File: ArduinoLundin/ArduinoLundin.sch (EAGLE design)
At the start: 24 parts, among them Q1 #MHz, U1 ATMEGA168#, U2 ###V

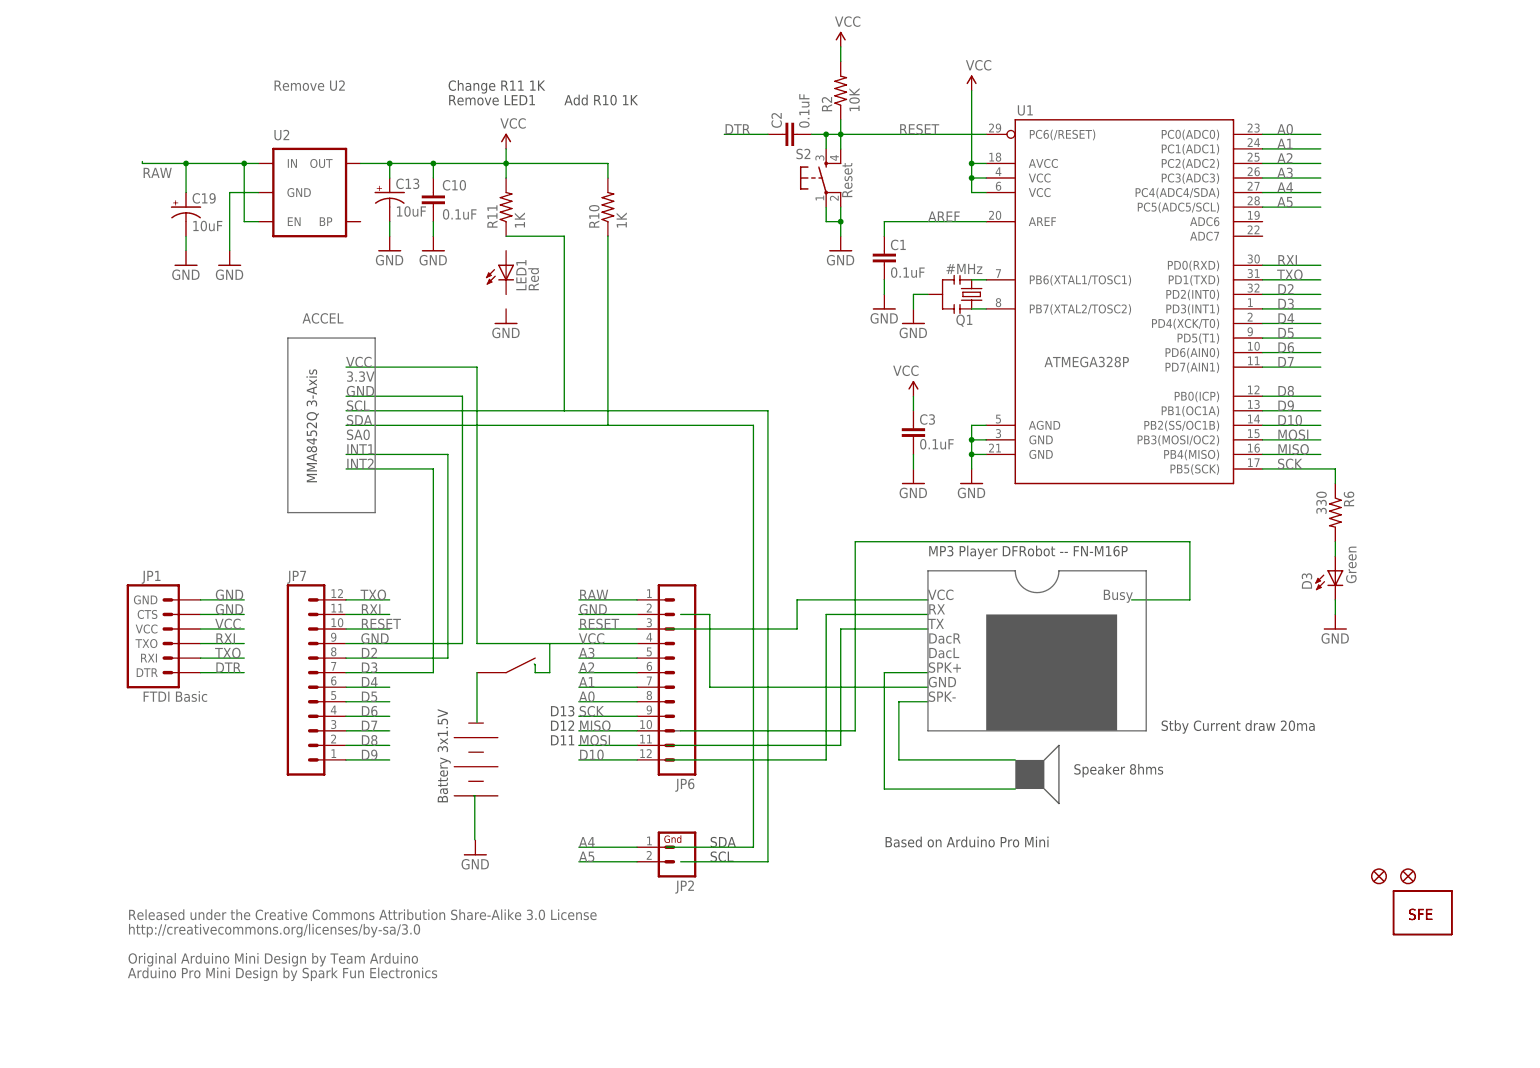
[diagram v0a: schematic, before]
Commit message: added power down option for MP3 and USB connector
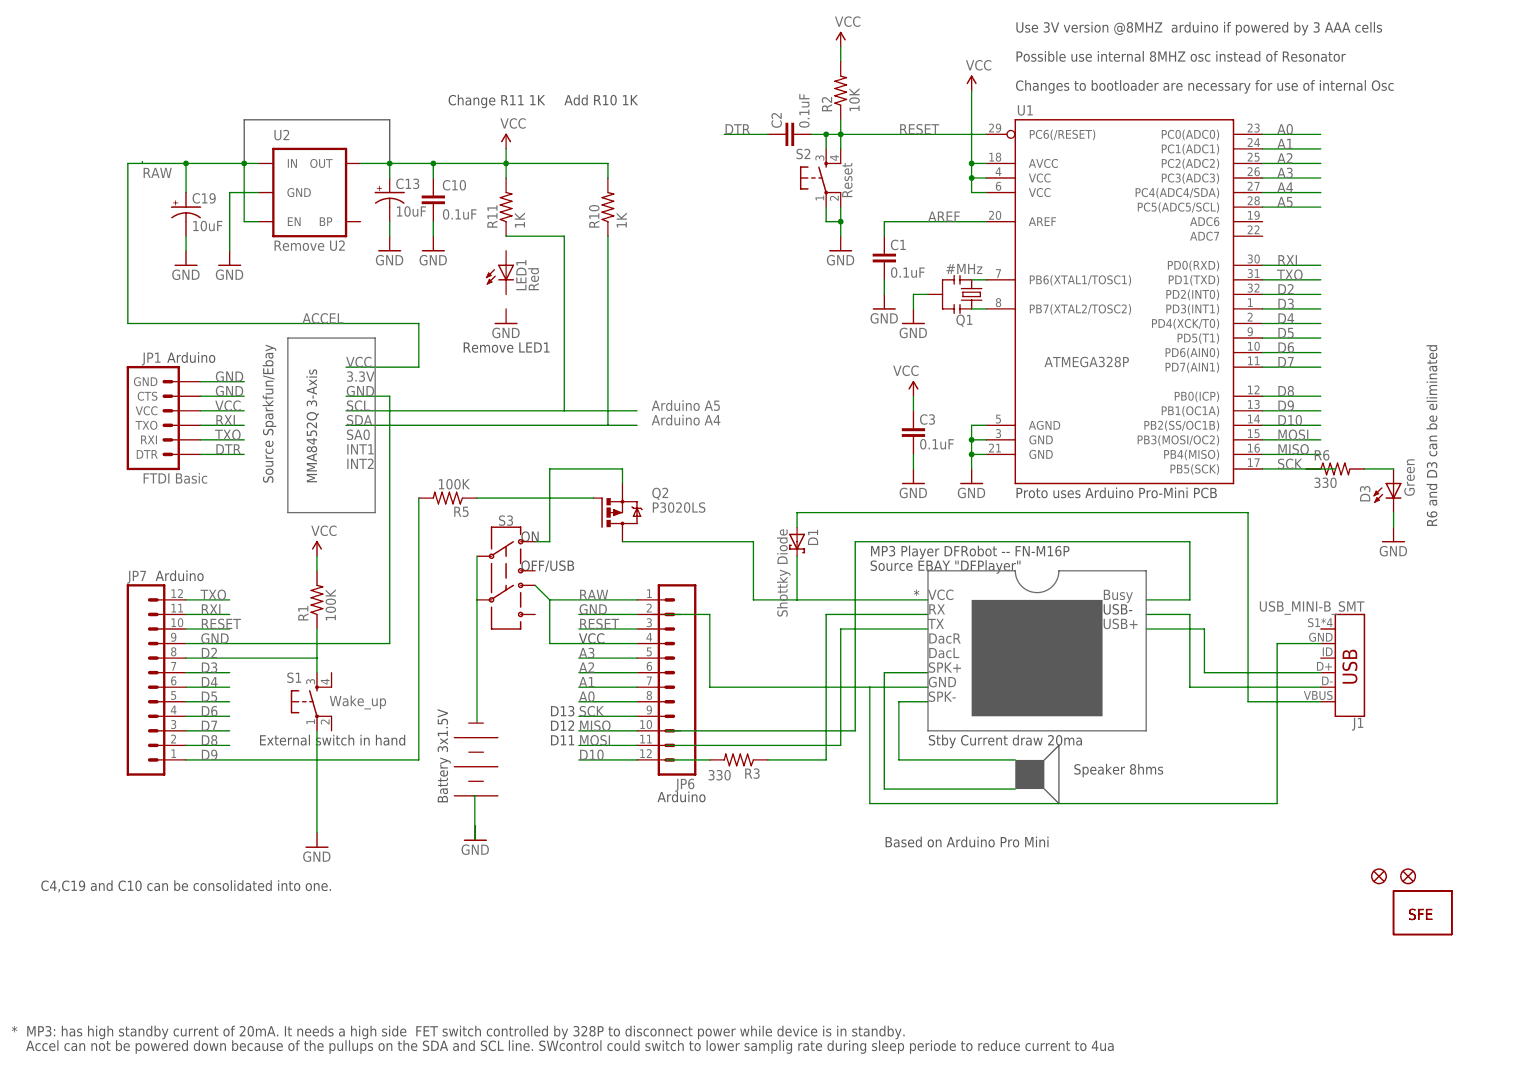
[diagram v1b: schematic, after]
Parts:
- removed JP2: (no value), SparkFun:M02PTH
- added D1: Shottky Diode, diode:BAS40
- added J1: USB_MINI-B_SMT, SparkFun-Connectors:USB_MINI-B_SMT
- added Q2: P3020LS, transistor-power:IRFR5305
- added R1, R5: 100K, SparkFun:RESISTOR0402
- added R3: 330, SparkFun:RESISTOR0402
- added S1: Wake_up, SparkFun:TAC_SWITCHSND
- added S3: (no value), SparkFun-Switches:SWITCH-DPDT-SMD-AYZ0202
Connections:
- new net 3.3V: R1.2
- new net N$11: D1.A, J1.VBUS
- new net N$12: R3.1
- new net N$16: S3.2, S3.5
- new net N$18: J1.D-
- new net N$19: J1.D+
- new net N$22: Q2.S, S3.1
- new net N$3: Q2.G, R5.1
- new net N$5: R3.2
- new net N$9: J1.GND
- net A4: no longer JP2.1
- net A5: no longer JP2.2
- net D2: now also R1.1, S1.3
- net D9: now also R5.2
- net GND: now also S1.1
- net RAW: now also JP6.4, S3.4
- net VCC: now also D1.C, Q2.D; no longer JP6.4
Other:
- note added: "*"
- note added: "Accel can not be powered down because of the pullups on the SDA and SCL line. SWcontrol could switch to lower samplig rate during sleep periode to reduce current to 4ua"
- note added: "Arduino"
- note added: "Arduino A4"
- note added: "Arduino A5"
- note added: "C4,C19 and C10 can be consolidated into one."
- note added: "Changes to bootloader are necessary for use of internal Osc"
- note added: "External switch in hand"
- note added: "MP3: has high standby current of 20mA. It needs a high side FET switch controlled by 328P to disconnect power while device is in standby."
- note added: "OFF/USB"
- note added: "ON"
- note added: "Possible use internal 8MHZ osc instead of Resonator"
- note added: "Proto uses Arduino Pro-Mini PCB"
- note added: "R6 and D3 can be eliminated"
- note added: "Source EBAY "DFPlayer""
- note added: "Source Sparkfun/Ebay"
- note added: "USB+"
- note added: "USB-"
- note added: "Use 3V version @8MHZ arduino if powered by 3 AAA cells"
- note removed: "Arduino Pro Mini Design by Spark Fun Electronics"
- note removed: "Original Arduino Mini Design by Team Arduino"
- note removed: "Released under the Creative Commons Attribution Share-Alike 3.0 License"
- note removed: "http://creativecommons.org/licenses/by-sa/3.0"
- moved on the sheet: D3, JP1, JP7, R6

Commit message: hopefully last changes
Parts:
- removed R10: 1K, SparkFun:RESISTOR0402
- added R7: 330, SparkFun:RESISTOR0402
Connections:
- removed net N$6: R11.1
- removed net N$8: R10.1
- new net N$17: R7.1
- new net N$20: R7.2
- net VCC: no longer R10.2
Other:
- note added: "Note: SCl,SDA pullups are on Accel module"
- note removed: "Add R10 1K"
- note removed: "Change R11 1K"
- note removed: "Stby Current draw 20ma"
- moved on the sheet: R3
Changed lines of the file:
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@@
 <part name="C2" library="SparkFun" deviceset="CAP" device="0402" value="0.1uF"/>
 <part name="GND2" library="SparkFun" deviceset="GND" device=""/>
-<part name="R10" library="SparkFun" deviceset="RESISTOR" device="0402" value="1K"/>
 <part name="S1" library="SparkFun" deviceset="TAC_SWITCH" device="SND" value="Wake_up"/>
 <part name="P+2" library="SparkFun" deviceset="3.3V" device="" value="VCC"/>
@@
 <part name="J1" library="SparkFun-Connectors" deviceset="USB_MINI-B" device="_SMT"/>
 <part name="D1" library="diode" deviceset="BAS40" device="" value="Shottky Diode"/>
+<part name="R7" library="SparkFun" deviceset="RESISTOR" device="0402" value="330"/>
 </parts>
 <sheets>
@@
 <wire x1="74.76870625" y1="49.613459375" x2="82.38870625" y2="49.613459375" width="0.1524" layer="94"/>
 <wire x1="77.30870625" y1="52.153459375" x2="79.84870625" y2="52.153459375" width="0.1524" layer="94"/>
-<text x="73.66" y="160.02" size="1.778" layer="97">Change R11 1K</text>
-<text x="93.98" y="160.02" size="1.778" layer="97">Add R10 1K</text>
 <text x="91.44" y="48.26" size="1.778" layer="97">D11</text>
 <text x="91.44" y="53.34" size="1.778" layer="97">D13</text>
@@
 <text x="73.66" y="38.1" size="1.778" layer="97" rot="R90">Battery 3x1.5V</text>
 <text x="149.86" y="30.48" size="1.778" layer="97">Based on Arduino Pro Mini </text>
-<text x="157.48" y="48.26" size="1.778" layer="97">Stby Current draw 20ma</text>
 <text x="177.8" y="114.3" size="1.778" layer="96">ATMEGA328P</text>
 <text x="172.72" y="172.72" size="1.778" layer="97">Use 3V version @8MHZ  arduino if powered by 3 AAA cells </text>
@@
 <text x="96.52" y="66.04" size="1.778" layer="97">VCC</text>
 <text x="172.72" y="162.56" size="1.778" layer="97">Changes to bootloader are necessary for use of internal Osc</text>
+<text x="66.04" y="109.22" size="1.778" layer="97">Note: SCl,SDA pullups are on Accel module</text>
 </plain>
 <instances>
@@
 </instance>
 <instance part="GND2" gate="1" x="78.458965625" y="31.696928125"/>
-<instance part="R10" gate="G$1" x="101.6" y="142.24" rot="R90"/>
 <instance part="S1" gate="S" x="50.8" y="55.88" smashed="yes" rot="R90">
 <attribute name="NAME" x="45.466" y="59.182" size="1.778" layer="95"/>
@@
 <instance part="R1" gate="G$1" x="50.8" y="73.66" rot="R90"/>
 <instance part="GND9" gate="1" x="50.8" y="30.48"/>
-<instance part="R3" gate="G$1" x="124.46" y="45.72" smashed="yes" rot="R180">
-<attribute name="NAME" x="128.27" y="44.2214" size="1.778" layer="95" rot="R180"/>
-<attribute name="VALUE" x="123.19" y="43.942" size="1.778" layer="96" rot="R180"/>
+<instance part="R3" gate="G$1" x="121.92" y="45.72" smashed="yes" rot="R180">
+<attribute name="NAME" x="125.73" y="44.2214" size="1.778" layer="95" rot="R180"/>
+<attribute name="VALUE" x="120.65" y="43.942" size="1.778" layer="96" rot="R180"/>
 </instance>
 <instance part="Q2" gate="G$1" x="101.6" y="88.9"/>
@@
 <instance part="J1" gate="G$1" x="231.14" y="63.5" rot="R180"/>
 <instance part="D1" gate="1" x="134.62" y="83.82" rot="R270"/>
+<instance part="R7" gate="G$1" x="132.08" y="48.26" smashed="yes" rot="R180">
+<attribute name="NAME" x="135.89" y="46.7614" size="1.778" layer="95" rot="R180"/>
+<attribute name="VALUE" x="130.81" y="46.482" size="1.778" layer="96" rot="R180"/>
+</instance>
 </instances>
 <busses>
@@
 <pinref part="C10" gate="G$1" pin="1"/>
 <pinref part="C13" gate="G$1" pin="+"/>
-<pinref part="R10" gate="G$1" pin="2"/>
-<wire x1="83.82" y1="149.86" x2="101.6" y2="149.86" width="0.1524" layer="91"/>
-<wire x1="101.6" y1="149.86" x2="101.6" y2="147.32" width="0.1524" layer="91"/>
 </segment>
 <segment>
@@
 <net name="N$6" class="0">
 <segment>
-<wire x1="55.88" y1="106.68" x2="93.98" y2="106.68" width="0.1524" layer="91"/>
-<wire x1="93.98" y1="106.68" x2="106.68" y2="106.68" width="0.1524" layer="91"/>
-<pinref part="R11" gate="G$1" pin="1"/>
-<wire x1="83.82" y1="137.16" x2="93.98" y2="137.16" width="0.1524" layer="91"/>
-<wire x1="93.98" y1="137.16" x2="93.98" y2="106.68" width="0.1524" layer="91"/>
+<wire x1="55.88" y1="106.68" x2="106.68" y2="106.68" width="0.1524" layer="91"/>
 </segment>
 </net>
 <net name="N$8" class="0">
 <segment>
-<wire x1="55.88" y1="104.14" x2="101.6" y2="104.14" width="0.1524" layer="91"/>
-<wire x1="101.6" y1="104.14" x2="106.68" y2="104.14" width="0.1524" layer="91"/>
-<pinref part="R10" gate="G$1" pin="1"/>
-<wire x1="101.6" y1="137.16" x2="101.6" y2="104.14" width="0.1524" layer="91"/>
+<wire x1="55.88" y1="104.14" x2="106.68" y2="104.14" width="0.1524" layer="91"/>
 </segment>
 </net>
@@
 <wire x1="139.7" y1="71.12" x2="157.48" y2="71.12" width="0.1524" layer="91"/>
 <pinref part="R3" gate="G$1" pin="1"/>
-<wire x1="129.54" y1="45.72" x2="139.7" y2="45.72" width="0.1524" layer="91"/>
+<wire x1="127" y1="45.72" x2="139.7" y2="45.72" width="0.1524" layer="91"/>
 </segment>
 </net>
@@
 <segment>
 <pinref part="R3" gate="G$1" pin="2"/>
-<wire x1="111.76" y1="45.72" x2="119.38" y2="45.72" width="0.1524" layer="91"/>
+<wire x1="111.76" y1="45.72" x2="116.84" y2="45.72" width="0.1524" layer="91"/>
 </segment>
 </net>
 <net name="N$17" class="0">
 <segment>
-<wire x1="111.76" y1="48.26" x2="142.24" y2="48.26" width="0.1524" layer="91"/>
 <wire x1="142.24" y1="48.26" x2="142.24" y2="68.58" width="0.1524" layer="91"/>
 <wire x1="142.24" y1="68.58" x2="157.48" y2="68.58" width="0.1524" layer="91"/>
+<pinref part="R7" gate="G$1" pin="1"/>
+<wire x1="137.16" y1="48.26" x2="142.24" y2="48.26" width="0.1524" layer="91"/>
 </segment>
 </net>
@@
 </segment>
 </net>
+<net name="N$20" class="0">
+<segment>
+<pinref part="R7" gate="G$1" pin="2"/>
+<wire x1="127" y1="48.26" x2="111.76" y2="48.26" width="0.1524" layer="91"/>
+</segment>
+</net>
